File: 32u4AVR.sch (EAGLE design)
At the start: 34 parts, among them IC1 MCP1252-33X50

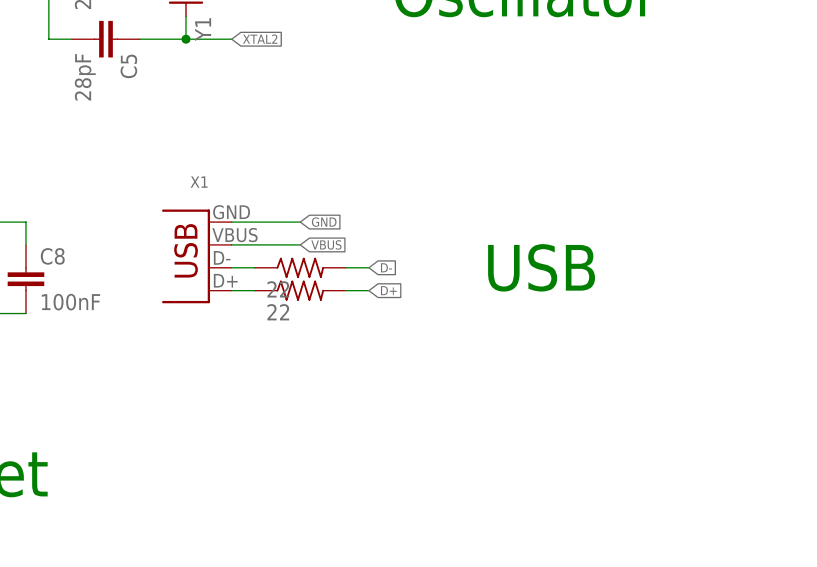
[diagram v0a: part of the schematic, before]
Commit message: Replaced USB A with micro USB
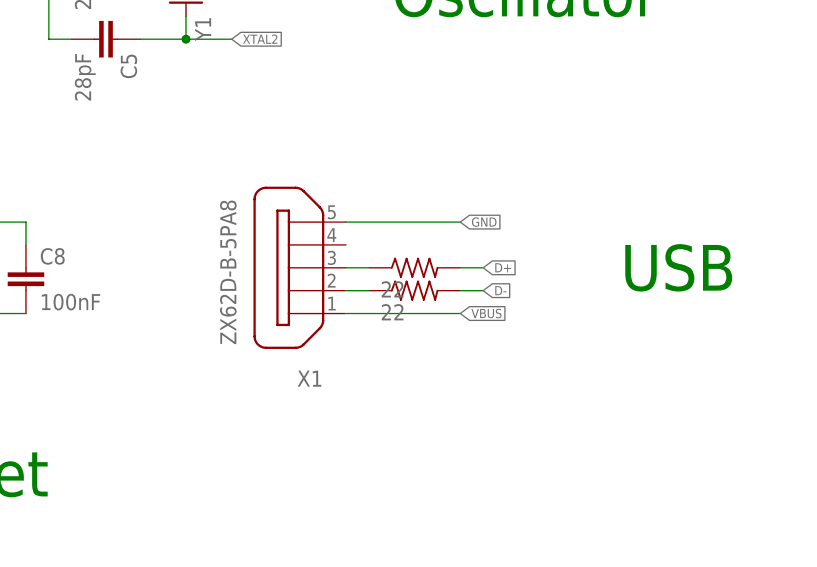
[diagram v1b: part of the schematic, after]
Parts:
- removed R1, R2: 22, resistor:R-US_R0402
- added R5, R6: 22, resistor:R-US_R0402
- X1: value (none) -> ZX62D-B-5PA8; device con-usb-3:USB-A-S -> zx62d-b-5pa8-oshpark_10:ZX62D-B-5PA8
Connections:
- net D+: now also R5.2; no longer R2.2
- net D-: now also R6.2; no longer R1.2
- net GND: now also X1G$1.5; no longer X1.GND
- net N$6: now also R6.1, X1G$1.2; no longer R1.1, X1.D-
- net N$7: now also R5.1, X1G$1.3; no longer R2.1, X1.D+
- net VBUS: now also X1G$1.1; no longer X1.VBUS
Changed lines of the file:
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@@
 <part name="U$1" library="AVR-ISP" deviceset="AVR-ISP" device=""/>
 <part name="IC1" library="microchip-MCP125x-xxx" deviceset="MCP1252-33X50" device=""/>
-<part name="X1" library="con-usb-3" deviceset="USB" device="-A-S"/>
 <part name="C1" library="resistor" library_urn="urn:adsk.eagle:library:348" deviceset="C-EU" device="C0402K" package3d_urn="urn:adsk.eagle:package:26199/1" value="1uF"/>
 <part name="C2" library="resistor" library_urn="urn:adsk.eagle:library:348" deviceset="C-EU" device="C0402K" package3d_urn="urn:adsk.eagle:package:26199/1" value="10uF"/>
@@
 <part name="BT3" library="SparkFun-Batteries" library_urn="urn:adsk.eagle:library:508" deviceset="BATTERY" device="-AA" package3d_urn="urn:adsk.eagle:package:37211/1" value="1.5V"/>
 <part name="BT4" library="SparkFun-Batteries" library_urn="urn:adsk.eagle:library:508" deviceset="BATTERY" device="-AA" package3d_urn="urn:adsk.eagle:package:37211/1" value="1.5V"/>
-<part name="R1" library="resistor" library_urn="urn:adsk.eagle:library:348" deviceset="R-US_" device="R0402" package3d_urn="urn:adsk.eagle:package:26058/1" value="22"/>
-<part name="R2" library="resistor" library_urn="urn:adsk.eagle:library:348" deviceset="R-US_" device="R0402" package3d_urn="urn:adsk.eagle:package:26058/1" value="22"/>
 <part name="Y1" library="AP_quad" deviceset="CRYSTAL" device="SMD"/>
 <part name="C4" library="resistor" library_urn="urn:adsk.eagle:library:348" deviceset="C-EU" device="C0402K" package3d_urn="urn:adsk.eagle:package:26199/1" value="28pF"/>
@@
 <part name="R4" library="resistor" library_urn="urn:adsk.eagle:library:348" deviceset="R-US_" device="R0402" package3d_urn="urn:adsk.eagle:package:26058/1" value="350"/>
 <part name="C15" library="resistor" library_urn="urn:adsk.eagle:library:348" deviceset="C-EU" device="C1206K" package3d_urn="urn:adsk.eagle:package:26202/1" value="100uF"/>
+<part name="R5" library="resistor" library_urn="urn:adsk.eagle:library:348" deviceset="R-US_" device="R0402" package3d_urn="urn:adsk.eagle:package:26058/1" value="22"/>
+<part name="R6" library="resistor" library_urn="urn:adsk.eagle:library:348" deviceset="R-US_" device="R0402" package3d_urn="urn:adsk.eagle:package:26058/1" value="22"/>
+<part name="X1" library="zx62d-b-5pa8-oshpark_10" deviceset="ZX62D-B-5PA8" device=""/>
 </parts>
 <sheets>
@@
 <text x="-88.9" y="109.22" size="5.08" layer="91">Breakout</text>
 <text x="121.92" y="58.42" size="5.08" layer="91">Oscillator</text>
-<text x="132.08" y="27.94" size="5.08" layer="91">USB</text>
+<text x="147.32" y="27.94" size="5.08" layer="91">USB</text>
 <text x="66.04" y="5.08" size="5.08" layer="91">Reset</text>
 <text x="-139.7" y="25.4" size="5.08" layer="91">Battery</text>
@@
 <attribute name="VALUE" x="-91.44" y="-22.86" size="1.27" layer="96"/>
 </instance>
-<instance part="X1" gate="G$1" x="101.6" y="35.56" smashed="yes" rot="R180">
-<attribute name="NAME" x="101.6" y="40.64" size="1.27" layer="95" rot="R180"/>
-</instance>
 <instance part="C1" gate="G$1" x="-83.82" y="12.7" smashed="yes" rot="R90">
 <attribute name="NAME" x="-84.201" y="14.224" size="1.778" layer="95" rot="R90"/>
@@
 <attribute name="VALUE" x="-53.34" y="32.258" size="1.778" layer="96" font="vector" rot="R180" align="top-center"/>
 </instance>
-<instance part="R1" gate="G$1" x="111.76" y="30.48" smashed="yes">
-<attribute name="VALUE" x="107.95" y="27.178" size="1.778" layer="96"/>
-</instance>
-<instance part="R2" gate="G$1" x="111.76" y="27.94" smashed="yes">
-<attribute name="VALUE" x="107.95" y="24.638" size="1.778" layer="96"/>
-</instance>
 <instance part="Y1" gate="G$1" x="99.06" y="60.96" smashed="yes" rot="R270">
 <attribute name="NAME" x="100.076" y="58.42" size="1.778" layer="95" rot="R270"/>
@@
 <attribute name="NAME" x="29.464" y="-19.939" size="1.778" layer="95"/>
 <attribute name="VALUE" x="29.464" y="-25.019" size="1.778" layer="96"/>
+</instance>
+<instance part="R5" gate="G$1" x="124.46" y="30.48" smashed="yes">
+<attribute name="VALUE" x="120.65" y="27.178" size="1.778" layer="96"/>
+</instance>
+<instance part="R6" gate="G$1" x="124.46" y="27.94" smashed="yes">
+<attribute name="VALUE" x="120.65" y="24.638" size="1.778" layer="96"/>
+</instance>
+<instance part="X1" gate="G$1" x="111.76" y="30.48" smashed="yes" rot="R180">
+<attribute name="NAME" x="114.3" y="19.05" size="1.778" layer="95" font="vector" rot="R180"/>
+<attribute name="VALUE" x="102.87" y="38.1" size="1.778" layer="96" font="vector" rot="R270"/>
 </instance>
 </instances>
@@
 </segment>
 <segment>
-<pinref part="X1" gate="G$1" pin="GND"/>
-<wire x1="104.14" y1="35.56" x2="111.76" y2="35.56" width="0.1524" layer="91"/>
-<label x="111.76" y="35.56" size="1.016" layer="95" xref="yes"/>
-</segment>
-<segment>
 <pinref part="U$1" gate="G$1" pin="GND"/>
 <wire x1="106.68" y1="86.36" x2="111.76" y2="86.36" width="0.1524" layer="91"/>
@@
 <label x="22.86" y="-25.4" size="1.27" layer="95" rot="R180" xref="yes"/>
 </segment>
+<segment>
+<wire x1="116.84" y1="35.56" x2="129.54" y2="35.56" width="0.1524" layer="91"/>
+<label x="129.54" y="35.56" size="1.016" layer="95" xref="yes"/>
+<pinref part="X1" gate="G$1" pin="5"/>
+</segment>
 </net>
 <net name="N$3" class="0">
@@
 </net>
 <net name="VBUS" class="0">
-<segment>
-<pinref part="X1" gate="G$1" pin="VBUS"/>
-<wire x1="104.14" y1="33.02" x2="111.76" y2="33.02" width="0.1524" layer="91"/>
-<label x="111.76" y="33.02" size="1.016" layer="95" xref="yes"/>
-</segment>
 <segment>
 <pinref part="C7" gate="G$1" pin="1"/>
@@
 <label x="-20.32" y="91.44" size="1.016" layer="95" rot="R180" xref="yes"/>
 </segment>
-</net>
-<net name="N$6" class="0">
-<segment>
-<pinref part="X1" gate="G$1" pin="D-"/>
-<pinref part="R1" gate="G$1" pin="1"/>
-<wire x1="104.14" y1="30.48" x2="106.68" y2="30.48" width="0.1524" layer="91"/>
-</segment>
-</net>
-<net name="N$7" class="0">
-<segment>
-<pinref part="R2" gate="G$1" pin="1"/>
-<pinref part="X1" gate="G$1" pin="D+"/>
-<wire x1="106.68" y1="27.94" x2="104.14" y2="27.94" width="0.1524" layer="91"/>
+<segment>
+<wire x1="116.84" y1="25.4" x2="129.54" y2="25.4" width="0.1524" layer="91"/>
+<label x="129.54" y="25.4" size="1.016" layer="95" xref="yes"/>
+<pinref part="X1" gate="G$1" pin="1"/>
 </segment>
 </net>
 <net name="D-" class="0">
-<segment>
-<pinref part="R1" gate="G$1" pin="2"/>
-<wire x1="116.84" y1="30.48" x2="119.38" y2="30.48" width="0.1524" layer="91"/>
-<label x="119.38" y="30.48" size="1.016" layer="95" xref="yes"/>
-</segment>
 <segment>
 <pinref part="U$3" gate="G$1" pin="D-"/>
@@
 <label x="-10.16" y="68.58" size="1.016" layer="95" rot="R180" xref="yes"/>
 </segment>
+<segment>
+<pinref part="R6" gate="G$1" pin="2"/>
+<wire x1="129.54" y1="27.94" x2="132.08" y2="27.94" width="0.1524" layer="91"/>
+<label x="132.08" y="27.94" size="1.016" layer="95" xref="yes"/>
+</segment>
 </net>
 <net name="D+" class="0">
-<segment>
-<pinref part="R2" gate="G$1" pin="2"/>
-<wire x1="116.84" y1="27.94" x2="119.38" y2="27.94" width="0.1524" layer="91"/>
-<label x="119.38" y="27.94" size="1.016" layer="95" xref="yes"/>
-</segment>
 <segment>
 <pinref part="U$3" gate="G$1" pin="D+"/>
 <wire x1="-5.08" y1="66.04" x2="-10.16" y2="66.04" width="0.1524" layer="91"/>
 <label x="-10.16" y="66.04" size="1.016" layer="95" rot="R180" xref="yes"/>
+</segment>
+<segment>
+<pinref part="R5" gate="G$1" pin="2"/>
+<wire x1="129.54" y1="30.48" x2="132.08" y2="30.48" width="0.1524" layer="91"/>
+<label x="132.08" y="30.48" size="1.016" layer="95" xref="yes"/>
 </segment>
 </net>
@@
 </segment>
 </net>
+<net name="N$6" class="0">
+<segment>
+<pinref part="X1" gate="G$1" pin="2"/>
+<pinref part="R6" gate="G$1" pin="1"/>
+<wire x1="116.84" y1="27.94" x2="119.38" y2="27.94" width="0.1524" layer="91"/>
+</segment>
+</net>
+<net name="N$7" class="0">
+<segment>
+<pinref part="R5" gate="G$1" pin="1"/>
+<pinref part="X1" gate="G$1" pin="3"/>
+<wire x1="119.38" y1="30.48" x2="116.84" y2="30.48" width="0.1524" layer="91"/>
+</segment>
+</net>
